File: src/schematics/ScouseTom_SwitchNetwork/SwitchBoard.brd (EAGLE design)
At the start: 172.7 x 97.5 mm, 86 parts, among them IC2 LT1763CDE-5, U1 ADUM1410ARWZ, U2 MCP73831, U3 TPS61090RSAR, X1 DSUB _T, X2 DSUB_B, X3 USB-MICROB

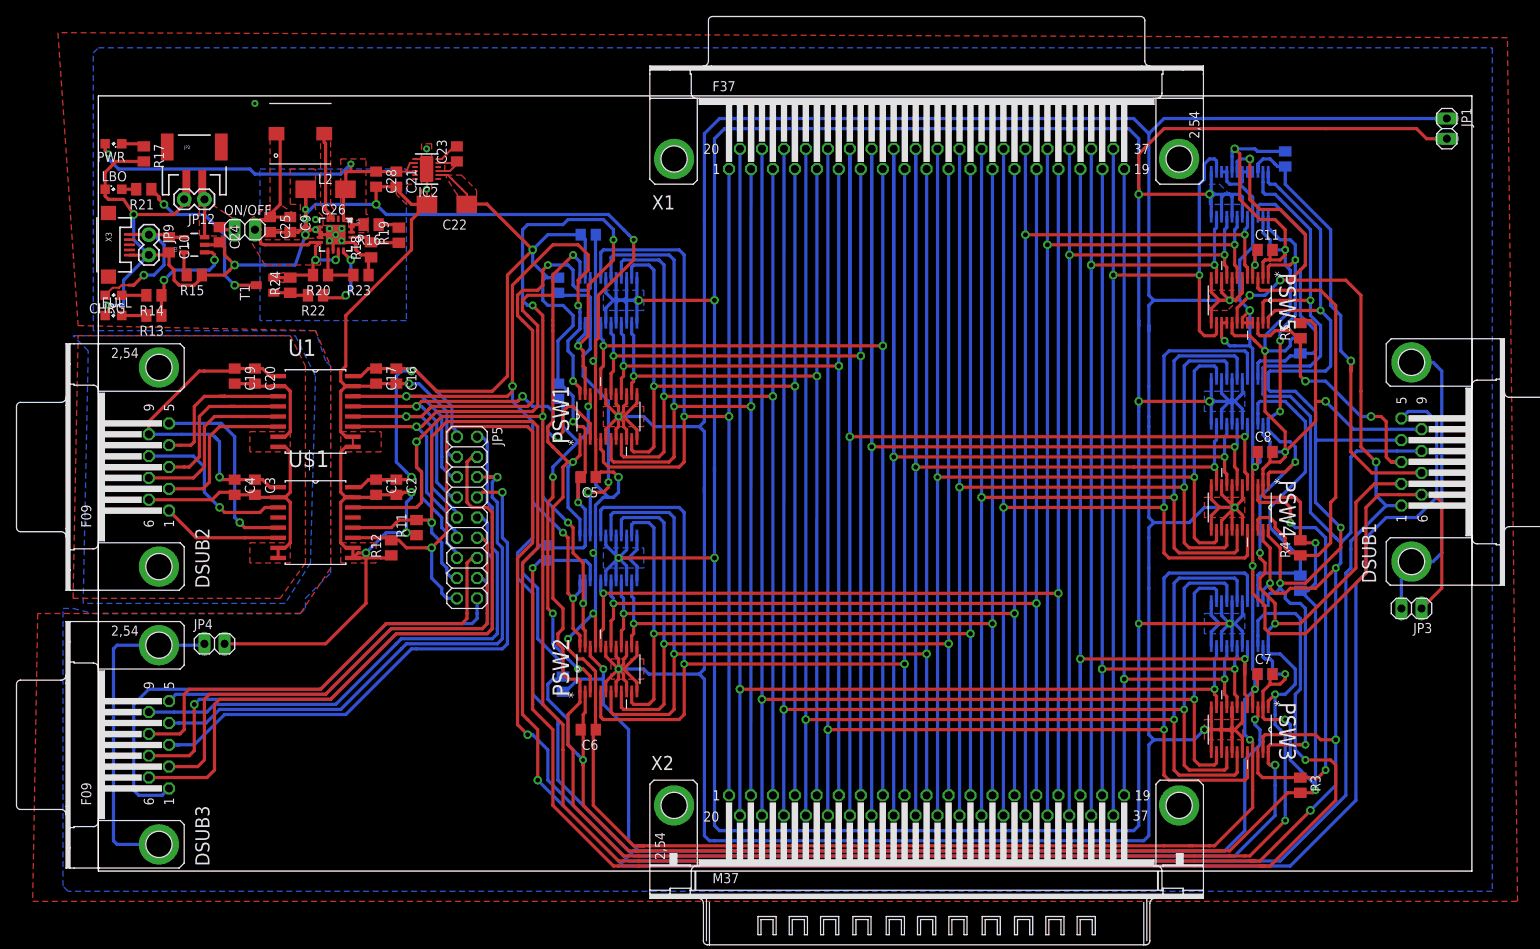
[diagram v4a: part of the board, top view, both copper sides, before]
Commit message: SwitchNetwork Finished. Gerber/BOM/P&P generated
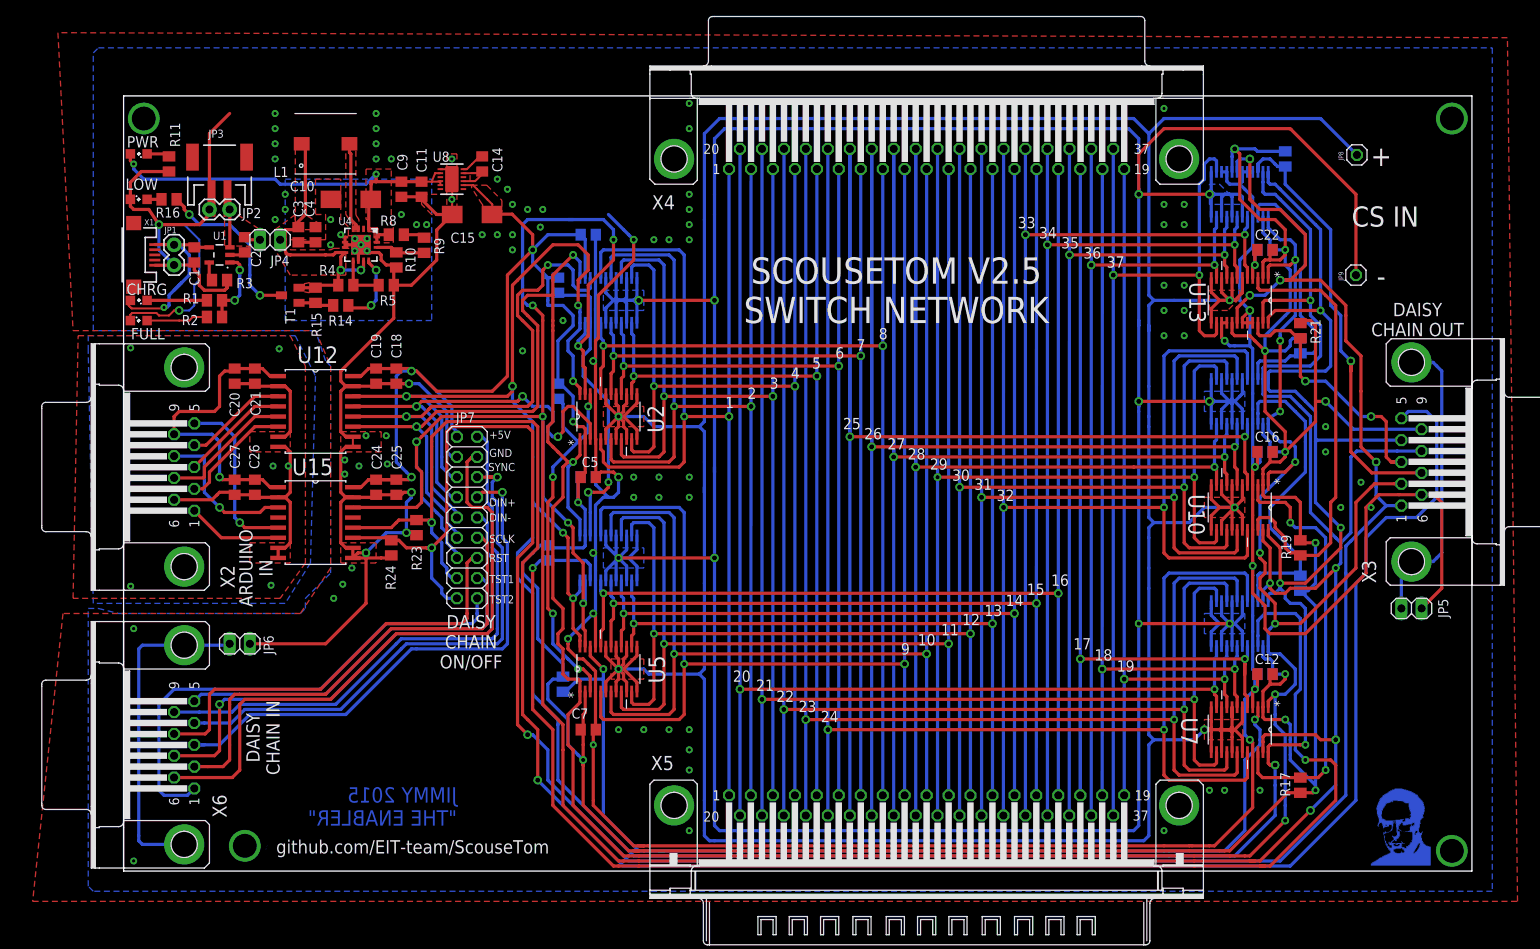
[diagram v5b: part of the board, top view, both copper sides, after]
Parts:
- removed C28: 2.2uF, resistor:C0805
- removed CHRG: YELLOW, led:SML0805
- removed DSUB1: CTR_OUT, con-subd:M09HP
- removed DSUB2: CTR_ARD, con-subd:F09HP
- removed DSUB3: CTR_IN, con-subd:F09HP
- removed FULL, LBO, PWR: GREEN, led:SML0805
- removed IC2: LT1763CDE-5, linear-technology:DFN12
- removed JP12: LiPoIN, SparkFun:1X02
- removed L2: 6.8uH, WE-PD:WE-PD_7332/7345_PLASTIC_BASE
- removed NSW1, PSW1: ADG714BRUZ, Analog Devices_By_element14_Batch_1:SOP65P640X120-24N
- removed ON/OFF: (no value), pinhead:1X02
- added C27: 1uF, resistor:C0805
- added JP6: Shld, pinhead:1X02
- added JP7: DCHN, pinhead:2X09
- added JP8: CS_IN+, pinhead:1X01
- added L1: 6.8uH, WE-PD:WE-PD_7332/7345_PLASTIC_BASE
- added LED1: YELLOW, led:SML0805
- added LED2, LED3: GREEN, led:SML0805
- added LED4: RED, led:SML0805
- added U12: ADUM1410ARWZ, ADI-Phase-2:SOIC127P1032X265-16N
- added U4: TPS61090RSAR, Adafruit PowerBoost 500C:QFN16-4X4
- added U8: LT1763CDE-5, linear-technology:DFN12
- added X4: DSUB _T, con-subd:F37HP
- added X5: DSUB_B, con-subd:M37HP
- added X6: CTR_IN, con-subd:F09HP
- C1, C3: value .1uF -> 10uF
- C10: value 10uF -> 100uF; device resistor:C0805 -> rcl:CT6032
- C11: value 0.1uF -> 10uF
- C14: value 0.1uF -> 0.01uF
- C15: value 0.1uF -> 100uF; device resistor:C0805 -> rcl:CT6032
- C16: value .1uF -> 0.1uF
- C17, C4: value 1uF -> 0.1uF
- C18: value 0.1uF -> .1uF
- C19: value .1uF -> 1uF
- C2: value 1uF -> 10uF
- C20: value 1uF -> .1uF
- C21, C25: value 10uF -> 1uF
- C22: value 100uF -> 0.1uF; device rcl:CT6032 -> resistor:C0805
- C23: value 0.01uF -> 0.1uF
- C24: value 10uF -> .1uF
- C26: value 100uF -> .1uF; device rcl:CT6032 -> resistor:C0805
- C9: value 0.1uF -> 2.2uF
- JP1: value (none) -> IN; device pinhead:1X02 -> SparkFun:1X02
- JP2: value LiPo -> LiPoIN; device SparkFun:JST-2-SMD -> SparkFun:1X02
- JP3: value (none) -> LiPo; device pinhead:1X02 -> SparkFun:JST-2-SMD
- JP4: value (none) -> PWR
- JP5: value (none) -> Shld; device pinhead:2X09 -> pinhead:1X02
- JP9: value IN -> CS_IN-; device SparkFun:1X02 -> pinhead:1X01
- R1: value 10k -> 470
- R10: value 10k -> 200k
- R11: value 10M -> 1k
- R12: value 10M -> 10k
- R13, R17, R21: value 1k -> 10k
- R14: value 470 -> 4.7k
- R15: value 2k -> 47k
- R16: value 1.8M -> 1k
- R18: value 200k -> 10k
- R19: value 82k -> 10k
- R2: value 10k -> 1k
- R20: value 2M -> 10k
- R22: value 4.7k -> 10k
- R23: value 360k -> 10M
- R24: value 47k -> 10M
- R3: value 10k -> 2k
- R4: value 10k -> 2M
- R5: value 10k -> 360k
- R8: value 10k -> 1.8M
- R9: value 10k -> 82k
- T1: value (none) -> PNP
- U1: value ADUM1410ARWZ -> MCP73831; device ADI-Phase-2:SOIC127P1032X265-16N -> SparkFun-PowerIC:SOT23-5
- U2: value MCP73831 -> ADG714BRUZ; device SparkFun:SOT23-5 -> Analog Devices_By_element14_Batch_1:SOP65P640X120-24N
- U3: value TPS61090RSAR -> ADG714BRUZ; device Adafruit PowerBoost 500C:QFN16-4X4 -> Analog Devices_By_element14_Batch_1:SOP65P640X120-24N
- X1: value DSUB _T -> USB-MICROB; device con-subd:F37HP -> SparkFun:USB-MICROB
- X2: value DSUB_B -> CTR_ARD; device con-subd:M37HP -> con-subd:F09HP
- X3: value USB-MICROB -> CTR_OUT; device SparkFun:USB-MICROB -> con-subd:M09HP
- moved X3 166.1 mm to (144.8, 55.9), turned to 90 degrees
- moved R17 165.7 mm to (130.8, 15.2)
- moved JP1 160.7 mm to (-10.8, 83.2)
- moved JP3 159.7 mm to (-5.08, 92.7), turned to 0 degrees
- moved JP9 151.9 mm to (137.8, 79.4), turned to 0 degrees
- moved R3 150.0 mm to (-5.08, 78.7), turned to 180 degrees
- moved R21 146.5 mm to (130.8, 72.4), turned to 90 degrees
- moved R4 124.5 mm to (10.8, 78.1), turned to 180 degrees
- moved R18 124.1 mm to (130.8, 40.6), flipped to the bottom, turned to 270 degrees
- moved R20 123.5 mm to (130.8, 70.5), flipped to the bottom, turned to 90 degrees
- moved R22 123.1 mm to (128.9, 94.0), flipped to the bottom, turned to 90 degrees
- moved R8 121.8 mm to (17.1, 84.5), flipped to the top, turned to 180 degrees
- moved R19 120.0 mm to (130.8, 45.1)
- moved JP5 119.3 mm to (144.8, 37.5), turned to 180 degrees
- moved C14 117.5 mm to (27.9, 93.3), flipped to the top, turned to 90 degrees
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- renumbered NSW2 to U6, NSW3 to U9, NSW4 to U11, NSW5 to U14, PSW2 to U5, PSW3 to U7, PSW4 to U10, PSW5 to U13, U$1 to U15
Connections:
- removed net N$2: CHRG.C, R14.2
- new net CHRG: LED1.C, R1.2
- net +5V: now also C21.1, C26.1, C27.1, U12.1, X2.9; no longer C19.1, C3.1, C4.1, DSUB2.9, U1.1
- net 5VIN: now also C1.1, JP1.1, LED1.A, U1.4, X1.VBUS; no longer C10.1, CHRG.A, JP9.1, U2.4, X3.VBUS
- net AGND: now also C10.-, C11.2, C15.-, C16.1, C17.1, C18.2, C19.2, C22.1, C23.1, C3.2, C4.2, JP1.2, JP2.2, JP5.1, JP6.2, JP7.3, LED2.C, LED4.C, R10.1, R11.2, R24.1, R3.1, R5.1, U1.2, U12.10, U12.15, U12.9, U2.21, U2.4, U3.21, U3.4, U4.10, U4.13, U4.5, U4.6, U4.7, U4.EXP, U8.7, U8.EXP, X1.GND, X3.6; no longer C10.2, C11.1, C14.1, C15.1, C16.2, C17.2, C18.1, C21.2, C22.-, C26.-, C28.2, DSUB1.6, FULL.C, IC2.7, IC2.EXP, JP12.2, JP2.1, JP4.2, JP5.3, JP9.2, LBO.C, NSW1.21, NSW1.4, PSW1.21, PSW1.4, R11.1, R12.1, R15.1, R17.2, R18.1, U1.10, U1.15, U1.9, U2.2, U3.10, U3.13, U3.5, U3.6, U3.7, U3.EXP, X3.GND
- net DIN+: now also JP7.7, U12.13, U2.3; no longer JP5.7, PSW1.3, U1.13
- net DIN+2: now also R6.1, U2.22; no longer PSW1.22, R1.1
- net DIN+3: now also R12.1; no longer R2.1
- net DIN+4: now also R17.1; no longer R3.1
- net DIN+5: now also R19.1; no longer R4.1
- net DIN+_DCHN: now also JP7.8, X6.3; no longer DSUB3.3, JP5.8
- net DIN+_IN: now also U12.4, X2.3; no longer DSUB2.3, U1.4
- net DIN-: now also JP7.9, U12.12, U3.3; no longer JP5.9, NSW1.3, U1.12
- net DIN-2: now also R7.1, U3.22; no longer NSW1.22, R6.1
- net DIN-3: now also R13.1; no longer R7.1
- net DIN-4: now also R18.1; no longer R8.1
- net DIN-5: now also R20.1; no longer R9.1
- net DIN-_DCHN: now also JP7.10, X6.7; no longer DSUB3.7, JP5.10
- net DIN-_IN: now also U12.5, X2.7; no longer DSUB2.7, U1.5
- net DOUT+: now also R21.1, X3.3; no longer DSUB1.3, R5.1
- net DOUT-: now also R22.1, X3.7; no longer DSUB1.7, R10.1
- net GND: now also C21.2, C26.2, C27.2, U12.2, U12.7, U12.8, X2.6; no longer C19.2, C3.2, C4.2, DSUB2.6, U1.2, U1.7, U1.8
- net GND_DCHN: now also JP7.4, X6.6; no longer DSUB3.6, JP5.4
- net IN+: now also JP8.1, U2.10, U2.12, U2.13, U2.15, U2.17, U2.19, U2.6, U2.8; no longer JP1.1, PSW1.10, PSW1.12, PSW1.13, PSW1.15, PSW1.17, PSW1.19, PSW1.6, PSW1.8
- net IN-: now also JP9.1, U3.10, U3.12, U3.13, U3.15, U3.17, U3.19, U3.6, U3.8; no longer JP1.2, NSW1.10, NSW1.12, NSW1.13, NSW1.15, NSW1.17, NSW1.19, NSW1.6, NSW1.8
- net LBO: now also R14.1, U4.12; no longer R22.1, U3.12
- net LB_REF: now also R4.1, R5.2, U4.9; no longer R20.1, R23.2, U3.9
- net N$10: now also JP5.2, X3.G1, X3.G2; no longer DSUB1.G1, DSUB1.G2, JP3.2
- net N$11: now also R14.2, R15.1; no longer R22.2, R24.1
- net N$12: now also JP6.1, X6.G1, X6.G2; no longer DSUB3.G1, DSUB3.G2, JP4.1
- net N$3: now also C14.1, U8.3, U8.5; no longer C23.1, IC2.3, IC2.5
- net N$4: now also C14.2, U8.6; no longer C23.2, IC2.6
- net N$5: now also LED2.A, R2.2; no longer FULL.A, R13.2
- net N$6: now also R8.1, R9.2; no longer R16.1, R19.2
- net N$7: now also LED3.C, R11.1; no longer PWR.C, R17.1
- net N$8: now also R16.1; no longer R21.1
- net N$9: now also LED4.A, R16.2; no longer LBO.A, R21.2
- net OUT_1: now also U2.5, U3.5, X4.1, X5.1; no longer NSW1.5, PSW1.5, X1.1, X2.1
- net OUT_10: now also X4.10, X5.10; no longer X1.10, X2.10
- net OUT_11: now also X4.11, X5.11; no longer X1.11, X2.11
- net OUT_12: now also X4.12, X5.12; no longer X1.12, X2.12
- net OUT_13: now also X4.13, X5.13; no longer X1.13, X2.13
- net OUT_14: now also X4.14, X5.14; no longer X1.14, X2.14
- net OUT_15: now also X4.15, X5.15; no longer X1.15, X2.15
- net OUT_16: now also X4.16, X5.16; no longer X1.16, X2.16
- net OUT_17: now also X4.17, X5.17; no longer X1.17, X2.17
- net OUT_18: now also X4.18, X5.18; no longer X1.18, X2.18
- net OUT_19: now also X4.19, X5.19; no longer X1.19, X2.19
- net OUT_2: now also U2.7, U3.7, X4.2, X5.2; no longer NSW1.7, PSW1.7, X1.2, X2.2
- net OUT_20: now also X4.20, X5.20; no longer X1.20, X2.20
- net OUT_21: now also X4.21, X5.21; no longer X1.21, X2.21
- net OUT_22: now also X4.22, X5.22; no longer X1.22, X2.22
- net OUT_23: now also X4.23, X5.23; no longer X1.23, X2.23
- net OUT_24: now also X4.24, X5.24; no longer X1.24, X2.24
- net OUT_25: now also X4.25, X5.25; no longer X1.25, X2.25
- net OUT_26: now also X4.26, X5.26; no longer X1.26, X2.26
- net OUT_27: now also X4.27, X5.27; no longer X1.27, X2.27
- net OUT_28: now also X4.28, X5.28; no longer X1.28, X2.28
- net OUT_29: now also X4.29, X5.29; no longer X1.29, X2.29
- net OUT_3: now also U2.9, U3.9, X4.3, X5.3; no longer NSW1.9, PSW1.9, X1.3, X2.3
- net OUT_30: now also X4.30, X5.30; no longer X1.30, X2.30
- net OUT_31: now also X4.31, X5.31; no longer X1.31, X2.31
- net OUT_32: now also X4.32, X5.32; no longer X1.32, X2.32
- net OUT_33: now also X4.33, X5.33; no longer X1.33, X2.33
- net OUT_34: now also X4.34, X5.34; no longer X1.34, X2.34
- net OUT_35: now also X4.35, X5.35; no longer X1.35, X2.35
- net OUT_36: now also X4.36, X5.36; no longer X1.36, X2.36
- net OUT_37: now also X4.37, X5.37; no longer X1.37, X2.37
- net OUT_4: now also U2.11, U3.11, X4.4, X5.4; no longer NSW1.11, PSW1.11, X1.4, X2.4
- net OUT_5: now also U2.14, U3.14, X4.5, X5.5; no longer NSW1.14, PSW1.14, X1.5, X2.5
- net OUT_6: now also U2.16, U3.16, X4.6, X5.6; no longer NSW1.16, PSW1.16, X1.6, X2.6
- net OUT_7: now also U2.18, U3.18, X4.7, X5.7; no longer NSW1.18, PSW1.18, X1.7, X2.7
- net OUT_8: now also U2.20, U3.20, X4.8, X5.8; no longer NSW1.20, PSW1.20, X1.8, X2.8
- net OUT_9: now also X4.9, X5.9; no longer X1.9, X2.9
- net PROG: now also R3.2, U1.5; no longer R15.2, U2.5
- net RESET_DCHN: now also JP7.14, X6.8; no longer DSUB3.8, JP5.14
- net RESET_IN: now also X2.8; no longer DSUB2.8
- net SCLK: now also JP7.11, U12.11, U2.1, U3.1, X3.2; no longer DSUB1.2, JP5.11, NSW1.1, PSW1.1, U1.11
- net SCLK_DCHN: now also JP7.12, X6.2; no longer DSUB3.2, JP5.12
- net SCLK_IN: now also U12.6, X2.2; no longer DSUB2.2, U1.6
- net STAT: now also R1.1, R2.1, U1.1; no longer R13.1, R14.1, U2.1
- net SW: now also L1.2, U4.3, U4.4; no longer L2.2, U3.3, U3.4
- net SYNC_DCHN: now also JP7.6, X6.4; no longer DSUB3.4, JP5.6
- net SYNC_IN: now also U12.3, X2.4; no longer DSUB2.4, U1.3
- net TEST_1: now also JP7.15, R23.2, X3.5; no longer DSUB1.5, JP5.15, R11.2
- net TEST_1_DCHN: now also JP7.16, X6.5; no longer DSUB3.5, JP5.16
- net TEST_1_IN: now also X2.5; no longer DSUB2.5
- net TEST_2: now also JP7.17, R24.2, X3.1; no longer DSUB1.1, JP5.17, R12.2
- net TEST_2_DCHN: now also JP7.18, X6.1; no longer DSUB3.1, JP5.18
- net TEST_2_IN: now also X2.1; no longer DSUB2.1
- net VBATT_A: now also C2.1, JP2.1, JP3.2, JP4.1, U1.3; no longer C24.1, JP12.1, JP2.2, ON/OFF.1, U2.3
- net VBATT_B: now also C3.1, C4.1, JP4.2, L1.1, R15.2, R4.2, U4.11, U4.8; no longer C25.1, C9.1, L2.1, ON/OFF.2, R20.2, R24.2, U3.11, U3.8
- net VDD: now also C15.+, C16.2, C17.2, C18.1, C19.1, C22.2, C23.2, C24.1, C25.1, JP7.1, R12.2, R13.2, R17.2, R18.2, R19.2, R20.2, R21.2, R22.2, U12.16, U2.2, U3.2, U8.2, X3.9; no longer C1.1, C11.2, C14.2, C15.2, C16.1, C17.1, C18.2, C2.1, C22.+, DSUB1.9, IC2.2, JP5.1, NSW1.2, PSW1.2, R1.2, R10.2, R2.2, R3.2, R4.2, R5.2, R8.2, R9.2, U1.16
- net VDD_DCHN: now also JP7.2, X6.9; no longer DSUB3.9, JP5.2
- net VREG: now also C10.+, C11.1, C9.1, LED3.A, R8.2, U4.1, U4.15, U4.16, U8.10, U8.11, U8.8; no longer C21.1, C26.+, C28.1, IC2.10, IC2.11, IC2.8, PWR.A, R16.2, U3.1, U3.15, U3.16
- net VSET: now also R10.2, R9.1, U4.14; no longer R18.2, R19.1, U3.14
- net ~RESET: now also JP7.13, U2.23, U3.23, X3.8; no longer DSUB1.8, JP5.13, NSW1.23, PSW1.23
- net ~SYNC: now also JP7.5, U12.14, U2.24, U3.24, X3.4; no longer DSUB1.4, JP5.5, NSW1.24, PSW1.24, U1.14
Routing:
- net AGND: track 668.2 -> 612.2 mm, vias 34 -> 109
- net IN+: track 511.5 -> 502.1 mm
- net CHRG: track 0.00 -> 7.52 mm
- net DIN+_IN: track 20.5 -> 13.7 mm
- net SYNC_IN: track 19.5 -> 13.1 mm
- net DIN-_IN: track 23.1 -> 17.0 mm
- net SCLK_IN: track 20.3 -> 14.5 mm
- net N$5: track 3.08 -> 7.71 mm
- net STAT: track 14.4 -> 9.77 mm
- net VBATT_B: track 40.0 -> 36.3 mm
- net 5VIN: track 20.9 -> 24.6 mm
- net +5V: track 43.1 -> 39.8 mm
- net TEST_2_IN: track 15.1 -> 12.0 mm
- net TEST_2_DCHN: track 66.1 -> 62.9 mm
- net TEST_1_DCHN: track 50.7 -> 47.5 mm
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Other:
- board size 172.7 x 97.5 mm -> 169.5 x 97.5 mm
- board text added: "+"
- board text added: "+5V"
- board text added: "-"
- board text added: "1"
- board text added: "10"
- board text added: "11"
- board text added: "12"
- board text added: "13"
- board text added: "14"
- board text added: "15"
- board text added: "16"
- board text added: "17"
- board text added: "18"
- board text added: "19"
- board text added: "2"
- board text added: "20"
- board text added: "21"
- board text added: "22"
- board text added: "23"
- board text added: "24"
- board text added: "25"
- board text added: "26"
- board text added: "27"
- board text added: "28"
- board text added: "29"
- board text added: "3"
- board text added: "30"
- board text added: "31"
- board text added: "32"
- board text added: "33"
- board text added: "34"
- board text added: "35"
- board text added: "36"
- board text added: "37"
- board text added: "4"
- board text added: "5"
- board text added: "6"
- board text added: "7"
- board text added: "8"
- board text added: "9"
- board text added: "ARDUINO IN"
- board text added: "CHRG"
- board text added: "CS IN"
- board text added: "DAISY CHAIN IN"
- board text added: "DAISY CHAIN ON/OFF"
- board text added: "DAISY CHAIN OUT"
- board text added: "DIN+"
- board text added: "DIN-"
- board text added: "FULL"
- board text added: "GND"
- board text added: "JIMMY 2015 "THE ENABLER""
- board text added: "LOW"
- board text added: "PWR"
- board text added: "RST"
- board text added: "SCLK"
- board text added: "SCOUSETOM V2.5 SWITCH NETWORK"
- board text added: "SYNC"
- board text added: "TO EEG"
- board text added: "TO ELECTRODES"
- board text added: "TST1"
- board text added: "TST2"
- board text added: "github.com/EIT-team/ScouseTom"
